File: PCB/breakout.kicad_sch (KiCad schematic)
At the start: 12 parts, among them J1 BKOUT_PINS, J2 POTENTIOMETER, U1 AD5293

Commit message: rev 0.0.0 final
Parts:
- added D3, D4: SD0805, Diode_SMD:D_0805_2012Metric, symbol Device:D_Schottky
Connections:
- net Vdd+: now also D4.1 (K); no longer J2.1 (Pin_1)
- net Vss-: now also D3.1 (K); no longer J2.5 (Pin_5)
- new net: D4.2 (A), J2.1 (Pin_1)
- new net: D3.2 (A), J2.5 (Pin_5)
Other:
- note added: "GND"
- note added: "H"
- note added: "HIPO"
- note added: "HOPI"
- note added: "L"
- note added: "RDY"
- note added: "SCK"
- note added: "Vcc"
- note added: "Vdd+"
- note added: "Vss-"
- note added: "W"
- note added: "~{CS}"
- note added: "~{RST}"
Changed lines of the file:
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@@
     (stroke (width 0) (type default) (color 0 0 0 0))
   )
-  (wire (pts (xy 187.96 81.915) (xy 187.96 93.345))
+  (wire (pts (xy 187.96 81.915) (xy 187.96 83.82))
     (stroke (width 0) (type default) (color 0 0 0 0))
   )
@@
     (stroke (width 0) (type default) (color 0 0 0 0))
   )
+  (wire (pts (xy 187.96 113.03) (xy 187.96 114.935))
+    (stroke (width 0) (type default) (color 0 0 0 0))
+  )
   (wire (pts (xy 48.895 174.625) (xy 52.705 174.625))
     (stroke (width 0) (type default) (color 0 0 0 0))
@@
     (stroke (width 0) (type default) (color 0 0 0 0))
   )
-  (wire (pts (xy 187.96 103.505) (xy 187.96 114.935))
+  (wire (pts (xy 187.96 103.505) (xy 187.96 105.41))
     (stroke (width 0) (type default) (color 0 0 0 0))
   )
@@
     (stroke (width 0) (type default) (color 0 0 0 0))
   )
+  (wire (pts (xy 187.96 91.44) (xy 187.96 93.345))
+    (stroke (width 0) (type default) (color 0 0 0 0))
+  )
   (wire (pts (xy 103.505 192.405) (xy 103.505 186.055))
     (stroke (width 0) (type default) (color 0 0 0 0))
   )
+  (text "Vss-" (at 201.295 104.14 0)
+    (effects (font (size 1.27 1.27)) (justify left bottom))
+  )
+  (text "Vcc" (at 75.565 92.075 180)
+    (effects (font (size 1.27 1.27)) (justify right bottom))
+  )
+  (text "RDY" (at 75.565 107.315 180)
+    (effects (font (size 1.27 1.27)) (justify right bottom))
+  )
+  (text "SCK" (at 75.565 97.155 180)
+    (effects (font (size 1.27 1.27)) (justify right bottom))
+  )
+  (text "~{CS}" (at 75.565 104.775 180)
+    (effects (font (size 1.27 1.27)) (justify right bottom))
+  )
+  (text "Vdd+" (at 201.295 93.98 0)
+    (effects (font (size 1.27 1.27)) (justify left bottom))
+  )
+  (text "GND" (at 201.295 106.68 0)
+    (effects (font (size 1.27 1.27)) (justify left bottom))
+  )
+  (text "W" (at 201.295 99.06 0)
+    (effects (font (size 1.27 1.27)) (justify left bottom))
+  )
   (text "Power Management" (at 76.835 165.1 0)
     (effects (font (size 1.27 1.27)) (justify left bottom))
   )
+  (text "HOPI" (at 75.565 102.235 180)
+    (effects (font (size 1.27 1.27)) (justify right bottom))
+  )
+  (text "GND" (at 75.565 94.615 180)
+    (effects (font (size 1.27 1.27)) (justify right bottom))
+  )
+  (text "~{RST}" (at 75.565 109.855 180)
+    (effects (font (size 1.27 1.27)) (justify right bottom))
+  )
+  (text "HIPO" (at 75.565 99.695 180)
+    (effects (font (size 1.27 1.27)) (justify right bottom))
+  )
+  (text "H" (at 201.295 96.52 0)
+    (effects (font (size 1.27 1.27)) (justify left bottom))
+  )
+  (text "L" (at 201.295 101.6 0)
+    (effects (font (size 1.27 1.27)) (justify left bottom))
+  )
   (label "W" (at 192.405 98.425 180)
     (effects (font (size 1.27 1.27)) (justify right bottom))
   )
-  (label "GND" (at 194.945 106.045 180)
+  (label "GND" (at 193.675 106.045 180)
     (effects (font (size 1.27 1.27)) (justify right bottom))
   )
@@
     (pin "1")
   )
+  (symbol (lib_id "Device:D_Schottky") (at 187.96 87.63 270) (unit 1)
+    (in_bom yes) (on_board yes)
+    (property "Reference" "D4" (id 0) (at 183.515 87.63 90)
+      (effects (font (size 1.27 1.27)) (justify left))
+    )
+    (property "Value" "SD0805" (id 1) (at 179.07 85.725 90)
+      (effects (font (size 1.27 1.27)) (justify left))
+    )
+    (property "Footprint" "Diode_SMD:D_0805_2012Metric" (id 2) (at 187.96 87.63 0)
+      (effects (font (size 1.27 1.27)) hide)
+    )
+    (property "Datasheet" "~" (id 3) (at 187.96 87.63 0)
+      (effects (font (size 1.27 1.27)) hide)
+    )
+    (pin "1")
+    (pin "2")
+  )
   (symbol (lib_id "Device:C_Small") (at 52.705 183.515 0) (unit 1)
     (in_bom yes) (on_board yes)
@@
     )
     (property "Datasheet" "~" (id 3) (at 52.705 183.515 0)
+      (effects (font (size 1.27 1.27)) hide)
+    )
+    (pin "1")
+    (pin "2")
+  )
+  (symbol (lib_id "Device:D_Schottky") (at 187.96 109.22 90) (unit 1)
+    (in_bom yes) (on_board yes)
+    (property "Reference" "D3" (id 0) (at 183.515 109.22 90)
+      (effects (font (size 1.27 1.27)) (justify right))
+    )
+    (property "Value" "SD0805" (id 1) (at 179.07 111.125 90)
+      (effects (font (size 1.27 1.27)) (justify right))
+    )
+    (property "Footprint" "Diode_SMD:D_0805_2012Metric" (id 2) (at 187.96 109.22 0)
+      (effects (font (size 1.27 1.27)) hide)
+    )
+    (property "Datasheet" "~" (id 3) (at 187.96 109.22 0)
       (effects (font (size 1.27 1.27)) hide)
     )
@@
       (reference "D1") (unit 1) (value "GRN") (footprint "LED_SMD:LED_0805_2012Metric")
     )
+    (path "/53c0f073-8749-45a1-a113-ffd7eac25629"
+      (reference "D3") (unit 1) (value "SD0805") (footprint "Diode_SMD:D_0805_2012Metric")
+    )
+    (path "/2a396d2f-1519-47b1-a6f7-3489c517a4a7"
+      (reference "D4") (unit 1) (value "SD0805") (footprint "Diode_SMD:D_0805_2012Metric")
+    )
     (path "/84916f83-d8a0-446a-8998-d523c09d50ab"

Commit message: initial repo load
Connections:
- net Vss-: now also D3.2 (A); no longer D3.1 (K)
- net at J2.5 (Pin_5): now also D3.1 (K); no longer D3.2 (A)
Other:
- moved on the sheet: D3
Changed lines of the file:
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@@
     (pin "2")
   )
-  (symbol (lib_id "Device:D_Schottky") (at 187.96 109.22 90) (unit 1)
+  (symbol (lib_id "Device:D_Schottky") (at 187.96 109.22 270) (unit 1)
     (in_bom yes) (on_board yes)
-    (property "Reference" "D3" (id 0) (at 183.515 109.22 90)
+    (property "Reference" "D3" (id 0) (at 186.69 107.95 90)
       (effects (font (size 1.27 1.27)) (justify right))
     )
-    (property "Value" "SD0805" (id 1) (at 179.07 111.125 90)
+    (property "Value" "SD0805" (id 1) (at 186.69 109.855 90)
       (effects (font (size 1.27 1.27)) (justify right))
     )

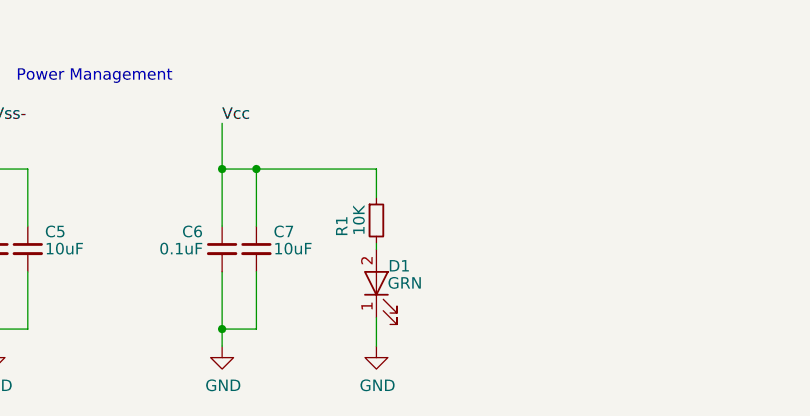
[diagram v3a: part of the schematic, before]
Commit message: add mounting holes; version 1.0.0
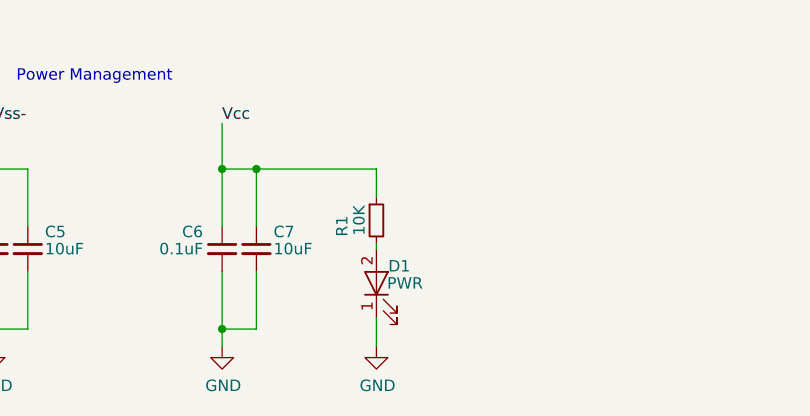
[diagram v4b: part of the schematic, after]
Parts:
- D1: value GRN -> PWR
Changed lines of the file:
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@@
     (title "AD5293_breakout")
     (date "2023-02-05")
-    (rev "0.0.0")
+    (rev "1.0.0")
     (company "Cedar Grove Studios")
   )
@@
     (in_bom yes) (on_board yes)
     (property "Reference" "D1" (id 0) (at 119.38 185.42 90))
-    (property "Value" "GRN" (id 1) (at 120.015 187.325 90))
+    (property "Value" "PWR" (id 1) (at 120.015 187.325 90))
     (property "Footprint" "LED_SMD:LED_0805_2012Metric" (id 2) (at 116.84 187.325 0)
       (effects (font (size 1.27 1.27)) hide)
@@
     )
     (path "/00000000-0000-0000-0000-00005c030d6d"
-      (reference "D1") (unit 1) (value "GRN") (footprint "LED_SMD:LED_0805_2012Metric")
+      (reference "D1") (unit 1) (value "PWR") (footprint "LED_SMD:LED_0805_2012Metric")
     )
     (path "/53c0f073-8749-45a1-a113-ffd7eac25629"

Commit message: refactor layout design; simplify routing
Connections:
- net GND: now also J2.1 (Pin_1); no longer J2.6 (Pin_6)
- net H: now also J2.5 (Pin_5); no longer J2.2 (Pin_2)
- net L: now also J2.3 (Pin_3); no longer J2.4 (Pin_4)
- net W: now also J2.4 (Pin_4); no longer J2.3 (Pin_3)
- net at D4.2 (A): now also J2.2 (Pin_2); no longer J2.1 (Pin_1)
- net at D3.1 (K): now also J2.6 (Pin_6); no longer J2.5 (Pin_5)
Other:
- moved on the sheet: D3, D4, J2

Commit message: update to ver 2.0.0
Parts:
- added R2, R3, R4: 10K, Resistor_SMD:R_0805_2012Metric, symbol breakout-rescue:R_Small-device
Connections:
- net HIPO: now also R4.2
- net RDY: now also R3.2
- net Vcc: now also R2.1, R3.1, R4.1
- net ~{RST}: now also R2.2

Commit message: update PCB design
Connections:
- net HIPO renamed SDO
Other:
- note added: "NOTE: SDO pin is not directly compatible with SPI HIPO unless tri-state buffered."
- note added: "SDO"
- note removed: "HIPO"
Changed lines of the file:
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@@
   (title_block
     (title "AD5293_breakout")
-    (date "2023-03-17")
-    (rev "2.0.0")
+    (date "2023-03-25")
+    (rev "2.0.1")
     (company "Cedar Grove Studios")
   )
@@
     (effects (font (size 1.27 1.27)) (justify right bottom))
   )
-  (text "HIPO" (at 75.565 99.695 180)
+  (text "SDO" (at 75.565 99.695 180)
     (effects (font (size 1.27 1.27)) (justify right bottom))
   )
@@
     (effects (font (size 1.27 1.27)) (justify left bottom))
   )
+  (text "NOTE: SDO pin is not directly\ncompatible with SPI HIPO unless\ntri-state buffered."
+    (at 89.535 85.725 0)
+    (effects (font (size 1.27 1.27)) (justify left bottom))
+  )
   (label "W" (at 192.405 98.425 180)
     (effects (font (size 1.27 1.27)) (justify right bottom))
@@
     (effects (font (size 1.27 1.27)) (justify right bottom))
   )
-  (label "HIPO" (at 98.425 99.06 180)
+  (label "SDO" (at 98.425 99.06 180)
     (effects (font (size 1.27 1.27)) (justify right bottom))
   )
@@
     (effects (font (size 1.27 1.27)) (justify left bottom))
   )
-  (label "HIPO" (at 123.19 93.345 0)
-    (effects (font (size 1.27 1.27)) (justify left bottom))
-  )
+  (label "SDO" (at 123.19 93.345 0)
+    (effects (font (size 1.27 1.27)) (justify left bottom))
+  )

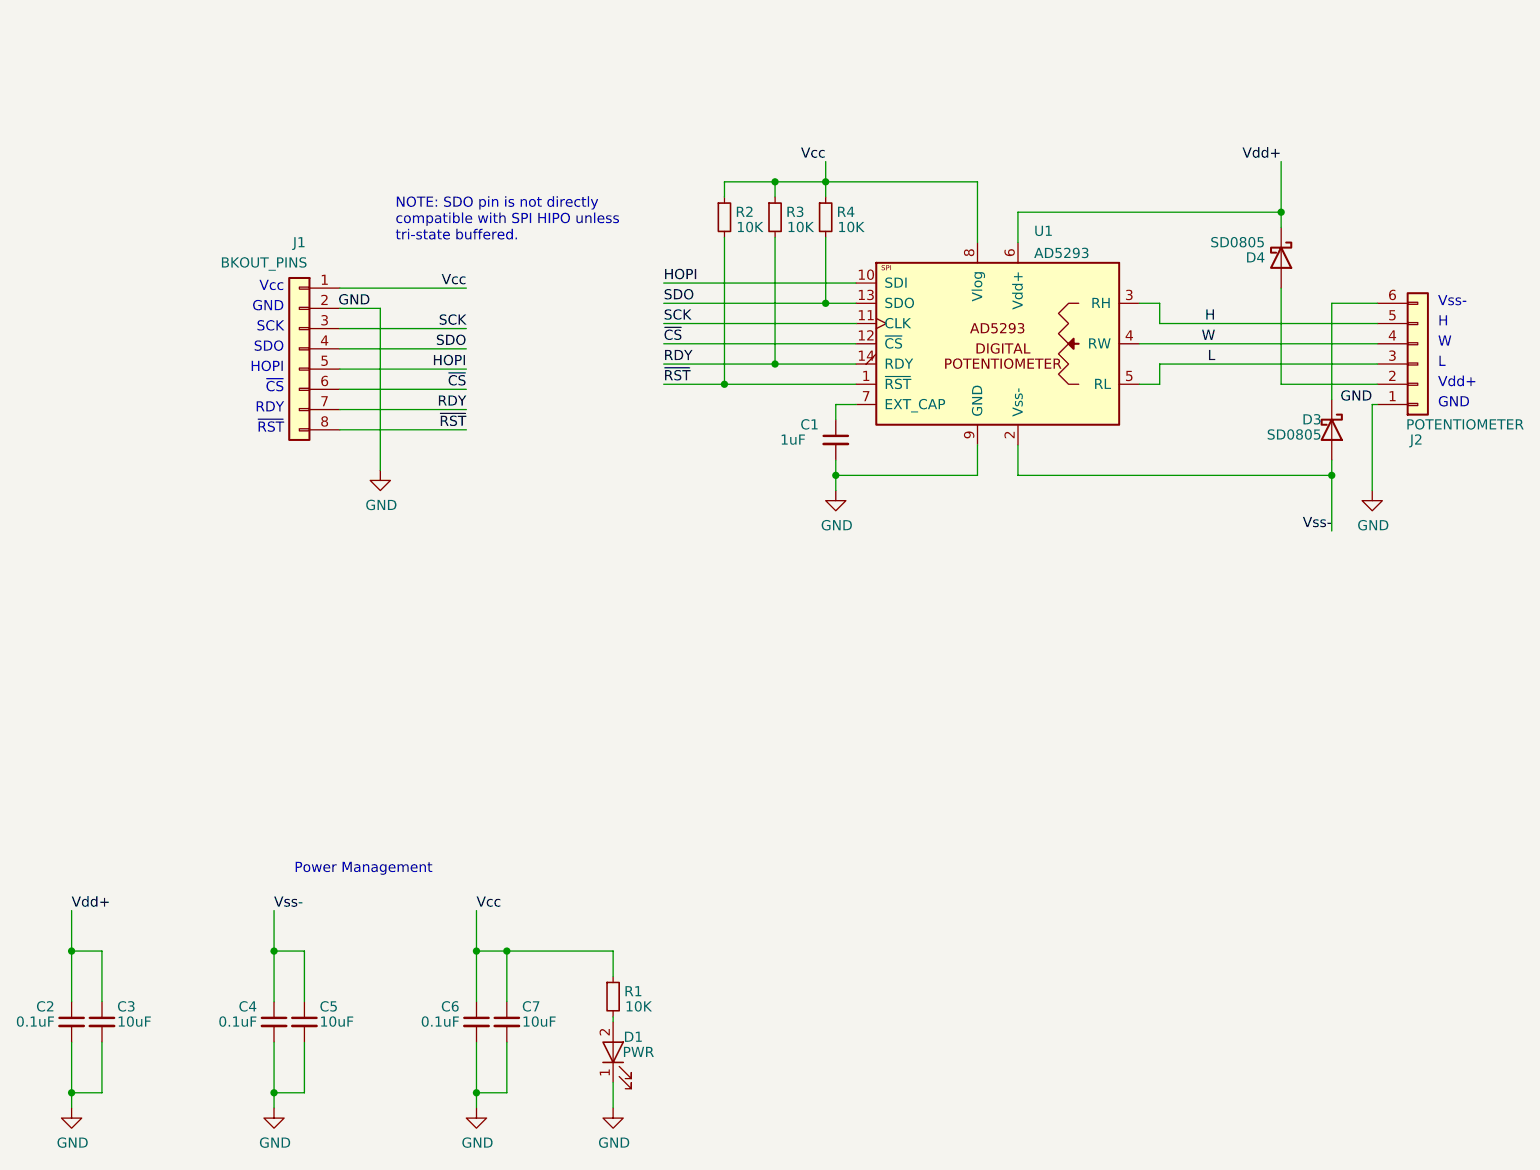
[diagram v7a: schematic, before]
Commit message: update design; add SDO pull-up jumper
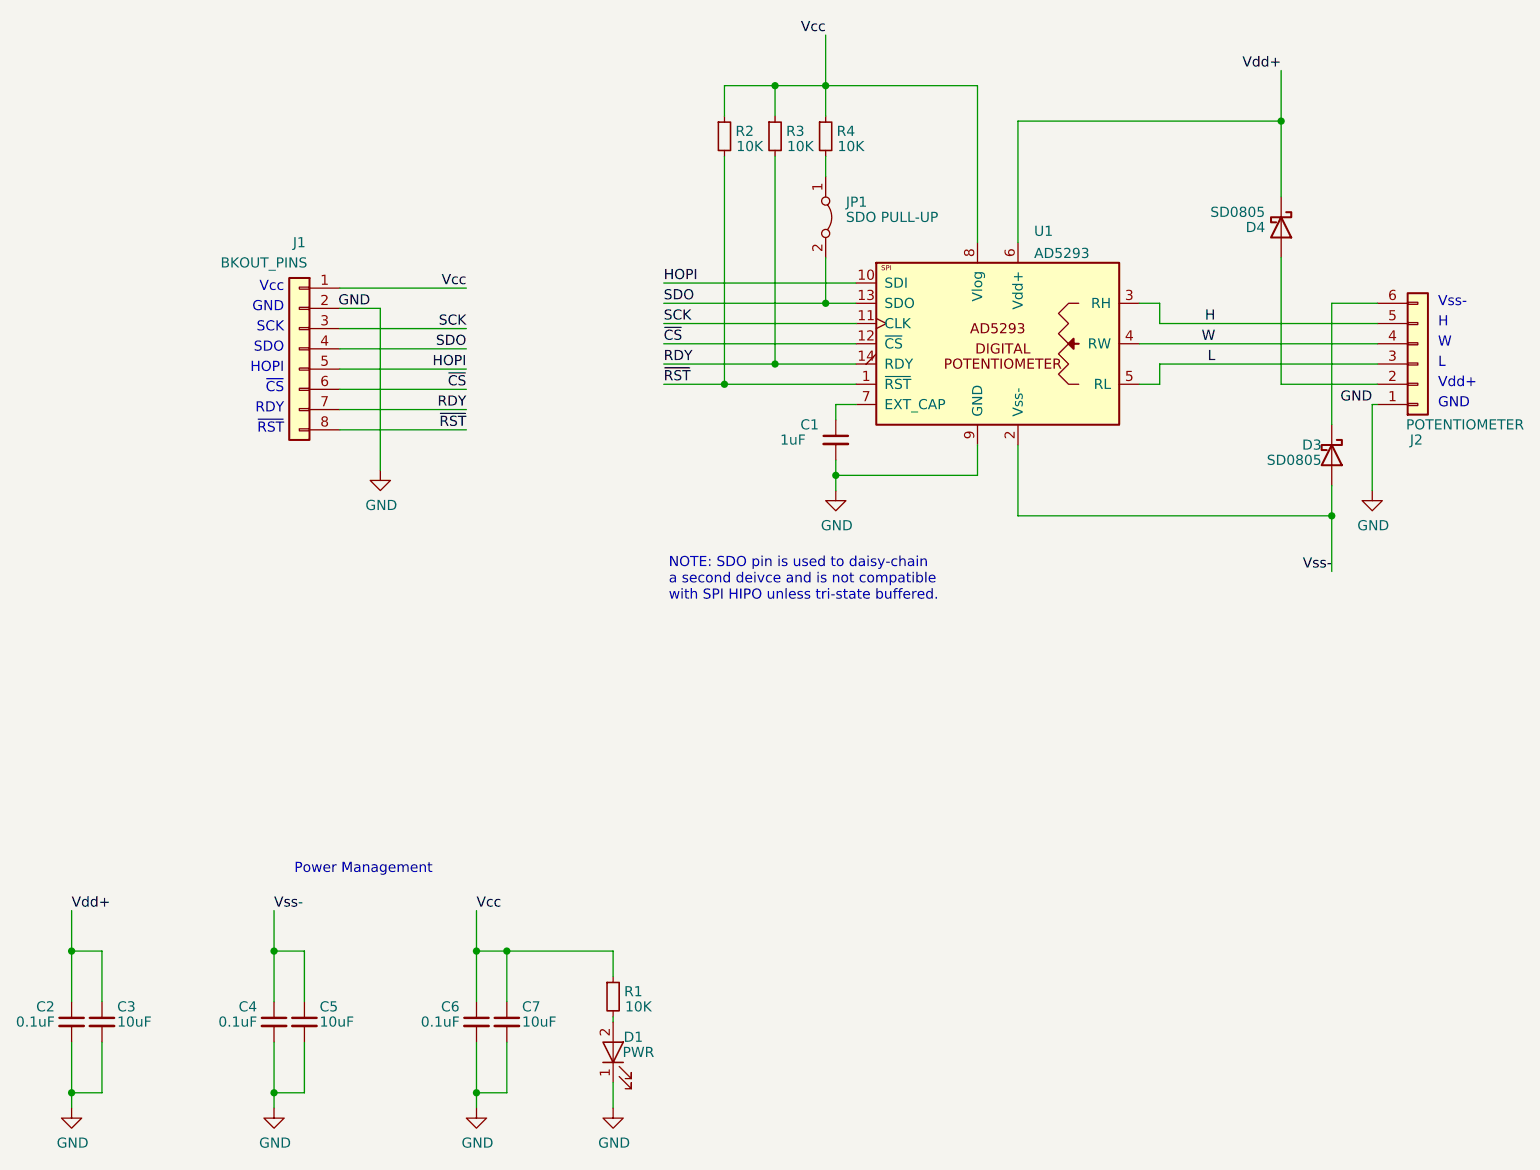
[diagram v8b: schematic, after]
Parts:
- added JP1: SDO PULL-UP, Jumper:SolderJumper-2_P1.3mm_Bridged_RoundedPad1.0x1.5mm, symbol Jumper:Jumper_2_Bridged
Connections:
- net SDO: now also JP1.2 (B); no longer R4.2
- new net: JP1.1 (A), R4.2
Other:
- note added: "NOTE: SDO pin is used to daisy-chain a second deivce and is not compatible with SPI HIPO unless tri-state buffered."
- note removed: "NOTE: SDO pin is not directly compatible with SPI HIPO unless tri-state buffered."
- moved on the sheet: D3, D4, R2, R3, R4
